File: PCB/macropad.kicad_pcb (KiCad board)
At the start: 2 copper layers, 80.5 x 95.5 mm, 38 parts, among them SW1 Kailh Choc V2, SW10 Kailh Choc V2, SW11 Kailh Choc V2, SW12 Kailh Choc V2, SW13 Kailh Choc V2, SW14 Kailh Choc V2, SW15 Kailh Choc V2, SW16 Kailh Choc V2, SW2 Kailh Choc V2, SW3 Kailh Choc V2, SW4 Kailh Choc V2, SW5 Kailh Choc V2, SW6 Kailh Choc V2, SW7 Kailh Choc V2, SW8 Kailh Choc V2, SW9 Kailh Choc V2, U2 SEEEDUINO XIAO RP2040

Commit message: Finish firmware + misc updates
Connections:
- Brd1 pad 2: +3.3V -> +5V
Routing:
- net +3.3V: track 28.4 -> 16.6 mm
- net +5V: track 76.7 -> 77.7 mm, vias 3 -> 2
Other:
- board text added: "Rev 5.2"
- board text removed: "Rev 5.1"
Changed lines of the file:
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@@
     (title "Cyao macropad")
     (date "2024-09-23")
-    (rev "v5.1")
+    (rev "v5.2")
     (company "Cheyao")
     (comment 1 "https://github.com/cheyao/macropad")
@@
       (net 26 "GND") (pinfunction "GND") (pintype "input"))
     (pad "2" thru_hole oval (at -1.08 -10.6 90) (size 2 1.6) (drill 1) (layers "*.Cu" "*.Mask")
-      (net 25 "+3.3V") (pinfunction "VCC") (pintype "input"))
+      (net 27 "+5V") (pinfunction "VCC") (pintype "input"))
     (pad "3" thru_hole oval (at 1.46 -10.6 90) (size 2 1.6) (drill 1) (layers "*.Cu" "*.Mask")
       (net 29 "Net-(Brd1-SCL)") (pinfunction "SCL") (pintype "input"))
@@
   (gr_line (start 185 145.5) (end 185 50)
     (stroke (width 0.05) (type default)) (layer "Edge.Cuts"))
-  (gr_text "Rev 5.1\n" (at 109.5 64.5) (layer "Eco2.User")
+  (gr_text "Rev 5.2\n\n" (at 109.5 69.25) (layer "Eco2.User")
     (effects (font (size 3 3) (thickness 0.3)) (justify left bottom))
   )
@@
   (segment (start 154 92.75) (end 152 92.75) (width 0.45) (layer "F.Cu") (net 5))
   (segment (start 179.46 60.46) (end 175.75 60.46) (width 0.45) (layer "F.Cu") (net 5))
-  (segment (start 177.12 95) (end 177.5 95) (width 0.45) (layer "F.Cu") (net 5))
   (segment (start 170.5 92.75) (end 168.5 92.75) (width 0.45) (layer "F.Cu") (net 5))
   (segment (start 152 92.75) (end 149.75 95) (width 0.45) (layer "F.Cu") (net 5))
@@
   (segment (start 174.16 52.84) (end 175.75 52.84) (width 0.45) (layer "B.Cu") (net 24))
   (segment (start 173.25 69.25) (end 173.25 53.75) (width 0.45) (layer "B.Cu") (net 24))
-  (segment (start 143.46 60.21) (end 146 62.75) (width 0.6) (layer "F.Cu") (net 25))
   (segment (start 146 62.75) (end 148.69 62.75) (width 0.6) (layer "F.Cu") (net 25))
   (segment (start 148.69 62.75) (end 148.75 62.81) (width 0.6) (layer "F.Cu") (net 25))
-  (segment (start 143.46 52) (end 143.46 60.21) (width 0.6) (layer "F.Cu") (net 25))
-  (segment (start 154.83 57.92) (end 160.5 57.92) (width 0.6) (layer "B.Cu") (net 25))
-  (segment (start 149.94 62.81) (end 154.83 57.92) (width 0.6) (layer "B.Cu") (net 25))
-  (segment (start 148.75 62.81) (end 149.94 62.81) (width 0.6) (layer "B.Cu") (net 25))
-  (segment (start 172.1 74.25) (end 172.2 74.15) (width 0.6) (layer "F.Cu") (net 26))
+  (segment (start 148.75 62.81) (end 150.94 62.81) (width 0.6) (layer "B.Cu") (net 25))
+  (segment (start 155.83 57.92) (end 160.5 57.92) (width 0.6) (layer "B.Cu") (net 25))
+  (segment (start 150.94 62.81) (end 155.83 57.92) (width 0.6) (layer "B.Cu") (net 25))
   (segment (start 126.45 73.8) (end 128 72.25) (width 0.6) (layer "F.Cu") (net 26))
   (segment (start 125.5 73.8) (end 126.45 73.8) (width 0.6) (layer "F.Cu") (net 26))
@@
   (via (at 171.5 60.5) (size 1) (drill 0.5) (layers "F.Cu" "B.Cu") (net 26))
   (via (at 172.25 72.75) (size 1) (drill 0.5) (layers "F.Cu" "B.Cu") (net 26))
+  (segment (start 140.92 56.42) (end 143.75 59.25) (width 0.6) (layer "B.Cu") (net 26))
   (segment (start 128 69.34) (end 140.92 56.42) (width 0.6) (layer "B.Cu") (net 26))
   (segment (start 128 72.25) (end 128 69.34) (width 0.6) (layer "B.Cu") (net 26))
-  (segment (start 154.12 55.38) (end 150.25 59.25) (width 0.6) (layer "B.Cu") (net 26))
-  (segment (start 143.75 59.25) (end 140.92 56.42) (width 0.6) (layer "B.Cu") (net 26))
+  (segment (start 143.75 59.25) (end 151 59.25) (width 0.6) (layer "B.Cu") (net 26))
   (segment (start 171.5 71.900002) (end 171.5 72) (width 0.6) (layer "B.Cu") (net 26))
+  (segment (start 154.87 55.38) (end 160.5 55.38) (width 0.6) (layer "B.Cu") (net 26))
   (segment (start 171.5 72) (end 172.25 72.75) (width 0.6) (layer "B.Cu") (net 26))
   (segment (start 140.92 56.42) (end 140.92 52) (width 0.6) (layer "B.Cu") (net 26))
-  (segment (start 150.25 59.25) (end 143.75 59.25) (width 0.6) (layer "B.Cu") (net 26))
-  (segment (start 160.5 55.38) (end 154.12 55.38) (width 0.6) (layer "B.Cu") (net 26))
+  (segment (start 151 59.25) (end 154.87 55.38) (width 0.6) (layer "B.Cu") (net 26))
   (segment (start 171.5 60.5) (end 171.5 71.900002) (width 0.6) (layer "B.Cu") (net 26))
-  (segment (start 156.66 52.84) (end 160.5 52.84) (width 0.6) (layer "F.Cu") (net 27))
   (segment (start 120.6 70.5) (end 120.6 69.9) (width 0.6) (layer "F.Cu") (net 27))
+  (segment (start 120.6 69.9) (end 134.29 56.21) (width 0.6) (layer "F.Cu") (net 27))
   (segment (start 169.25 68.75) (end 169.25 68.9) (width 0.6) (layer "F.Cu") (net 27))
   (segment (start 169.25 68.9) (end 167.3 70.85) (width 0.6) (layer "F.Cu") (net 27))
-  (segment (start 120.6 69.9) (end 122 68.5) (width 0.6) (layer "F.Cu") (net 27))
-  (segment (start 155.5 54) (end 156.66 52.84) (width 0.6) (layer "F.Cu") (net 27))
-  (segment (start 124.5 66) (end 149.75 66) (width 0.6) (layer "F.Cu") (net 27))
-  (segment (start 155.5 61.25) (end 155.5 54) (width 0.6) (layer "F.Cu") (net 27))
-  (segment (start 122 68.5) (end 124.5 66) (width 0.6) (layer "F.Cu") (net 27))
-  (via (at 149.75 66) (size 1) (drill 0.5) (layers "F.Cu" "B.Cu") (net 27))
-  (via (at 155.5 61.25) (size 1) (drill 0.5) (layers "F.Cu" "B.Cu") (net 27))
+  (segment (start 134.29 56.21) (end 143.46 56.21) (width 0.6) (layer "F.Cu") (net 27))
+  (via (at 143.46 56.21) (size 1) (drill 0.5) (layers "F.Cu" "B.Cu") (net 27))
   (via (at 169.25 68.75) (size 1) (drill 0.5) (layers "F.Cu" "B.Cu") (net 27))
+  (segment (start 155.16 52.84) (end 160.5 52.84) (width 0.6) (layer "B.Cu") (net 27))
   (segment (start 164.59 52.84) (end 160.5 52.84) (width 0.6) (layer "B.Cu") (net 27))
-  (segment (start 150.75 66) (end 155.5 61.25) (width 0.6) (layer "B.Cu") (net 27))
   (segment (start 169.25 57.5) (end 164.59 52.84) (width 0.6) (layer "B.Cu") (net 27))
-  (segment (start 149.75 66) (end 150.75 66) (width 0.6) (layer "B.Cu") (net 27))
+  (segment (start 143.46 56.21) (end 144.75 57.5) (width 0.6) (layer "B.Cu") (net 27))
+  (segment (start 144.75 57.5) (end 150.5 57.5) (width 0.6) (layer "B.Cu") (net 27))
+  (segment (start 143.46 52) (end 143.46 56.21) (width 0.6) (layer "B.Cu") (net 27))
+  (segment (start 150.5 57.5) (end 155.16 52.84) (width 0.6) (layer "B.Cu") (net 27))
   (segment (start 169.25 68.75) (end 169.25 57.5) (width 0.6) (layer "B.Cu") (net 27))
   (segment (start 151.25 56.25) (end 153.75 58.75) (width 0.45) (layer "F.Cu") (net 28))

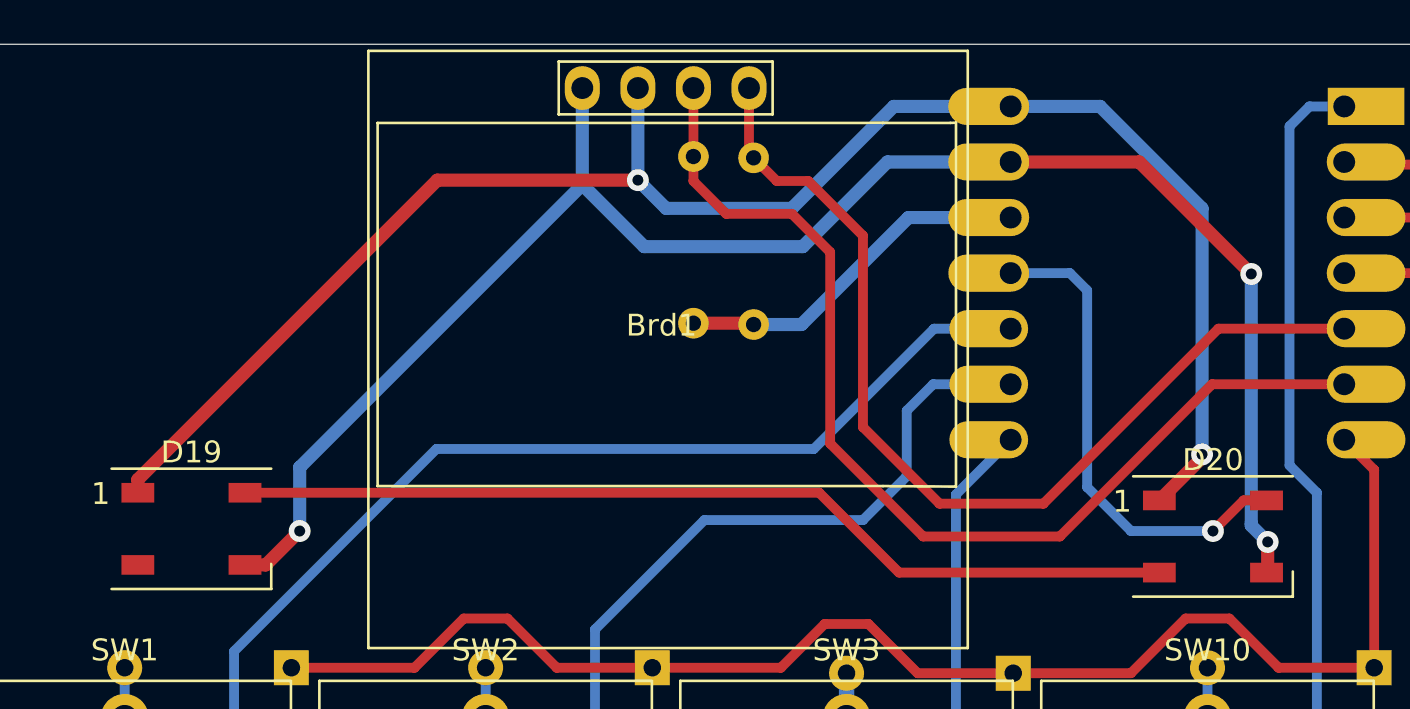
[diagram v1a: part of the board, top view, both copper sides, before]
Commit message: Add decoupling capacitors & verified footprints
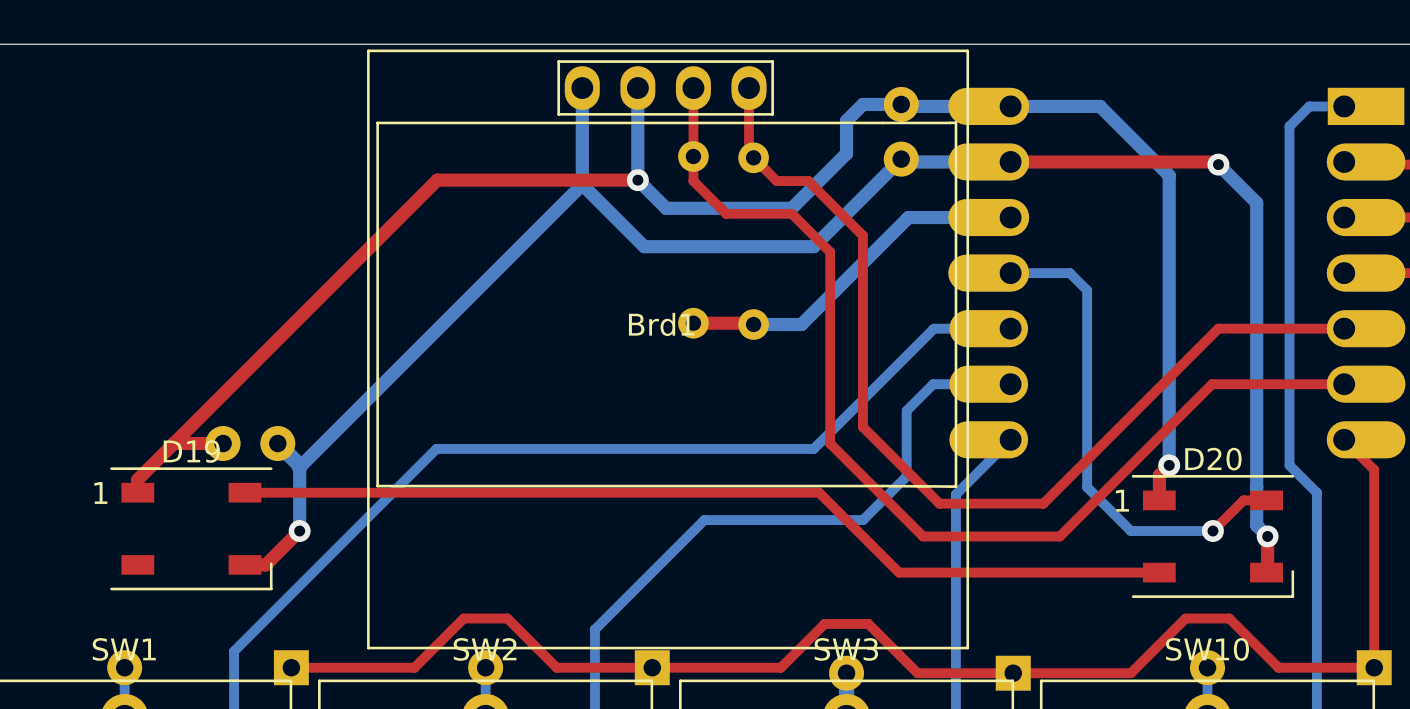
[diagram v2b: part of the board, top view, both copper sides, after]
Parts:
- added C1: 10pF, Capacitor_THT:C_Disc_D3.0mm_W1.6mm_P2.50mm, B.Cu at (124.5, 68.2)
- added C2: 1uF, Capacitor_THT:C_Disc_D3.0mm_W1.6mm_P2.50mm, B.Cu at (155.5, 52.8)
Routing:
- net GND: track 78.2 -> 81.9 mm
- net +5V: track 77.7 -> 79.6 mm
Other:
- board text added: "Rev 5.3"
- board text removed: "Rev 5.2"

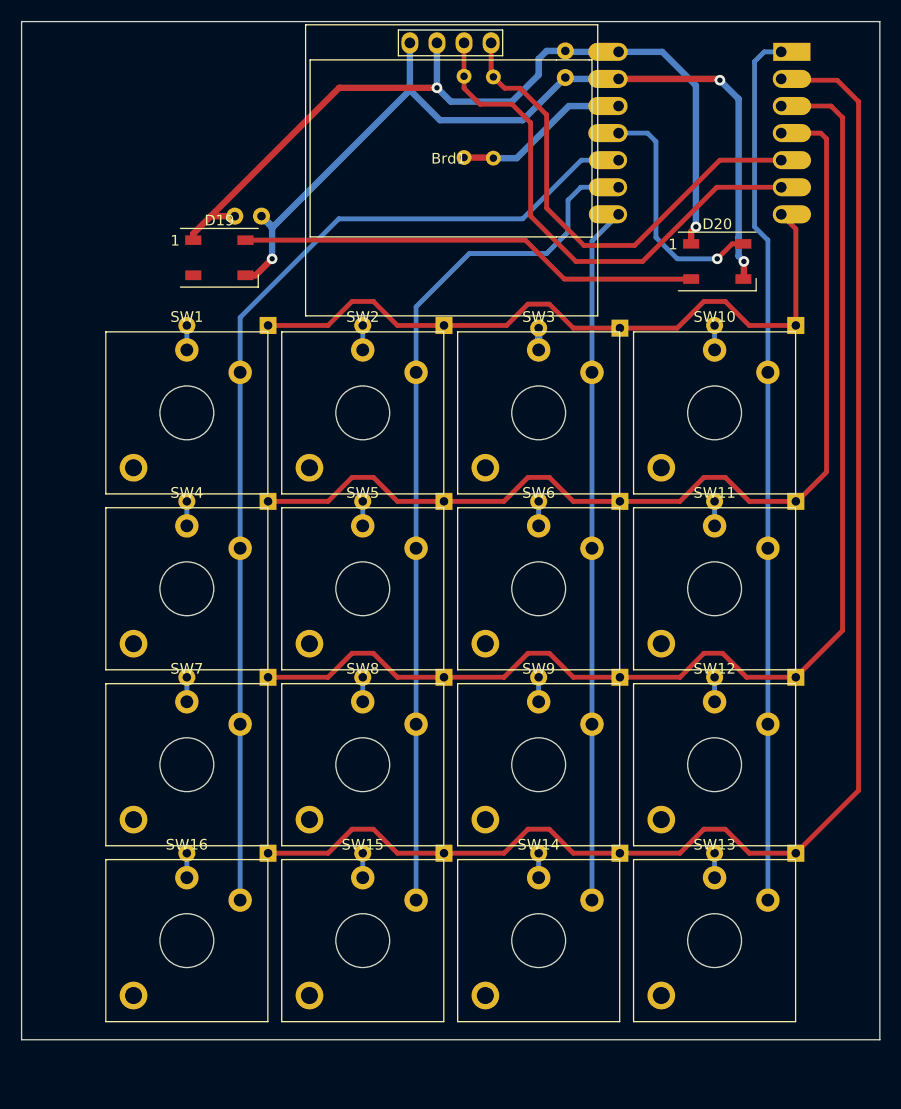
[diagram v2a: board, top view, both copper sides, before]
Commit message: Revamp switch margins
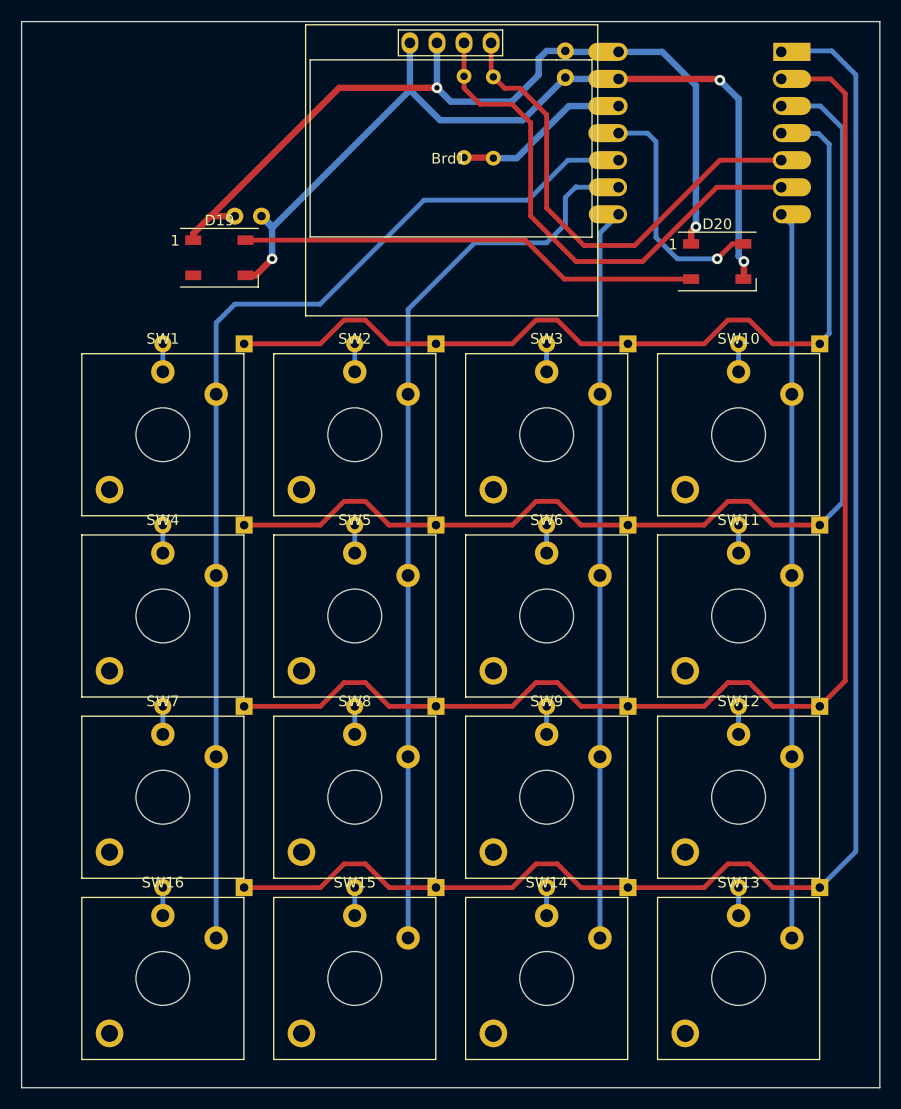
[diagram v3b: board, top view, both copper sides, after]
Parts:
- SW1, SW10, SW11, SW12, SW13, SW14, SW15, SW16, SW2, SW3, SW4, SW5, SW6, SW7, SW8, SW9: footprint key:SW_Kailh_Choc_V2 -> key:SW_Kailh_Choc_V2_1.00u
- moved SW13 4.20 mm to (171.8, 139.8)
- moved SW16 4.20 mm to (117.8, 139.8)
- moved D13 3.93 mm to (179.4, 131.2)
- moved D16 3.93 mm to (125.4, 131.2)
- moved SW12 3.79 mm to (171.8, 122.8)
- moved SW7 3.79 mm to (117.8, 122.8)
- moved SW14 3.63 mm to (153.8, 139.8)
- moved SW15 3.63 mm to (135.8, 139.8)
- moved D12 3.53 mm to (179.4, 114.2)
- moved D7 3.53 mm to (125.4, 114.2)
- moved SW11 3.40 mm to (171.8, 105.8)
- moved SW4 3.40 mm to (117.8, 105.8)
- moved D14 3.31 mm to (161.4, 131.2)
- moved D15 3.31 mm to (143.4, 131.2)
- moved D11 3.16 mm to (179.4, 97.2)
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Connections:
- U2 pad 1: COL3 -> ROW3
- U2 pad 2: ROW3 -> ROW2
- U2 pad 3: ROW2 -> ROW1
- U2 pad 4: ROW1 -> ROW0
- U2 pad 7: ROW0 -> COL3
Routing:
- net ROW0: track 66.1 -> 83.6 mm
- net COL3: track 82.0 -> 68.3 mm
- net ROW1: track 94.8 -> 104.2 mm
- net ROW3: track 136.2 -> 145.1 mm
- net ROW2: track 115.6 -> 124.6 mm
- net COL0: track 96.3 -> 101.8 mm
- net COL1: track 81.1 -> 84.9 mm
- net COL2: track 65.4 -> 68.6 mm
- net Net-(D3-A): track 2.05 -> 2.62 mm
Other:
- board size 80.5 x 95.5 mm -> 80.5 x 100 mm
- board text added: "Rev 6.0"
- board text removed: "Rev 5.3"

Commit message: Added backlights
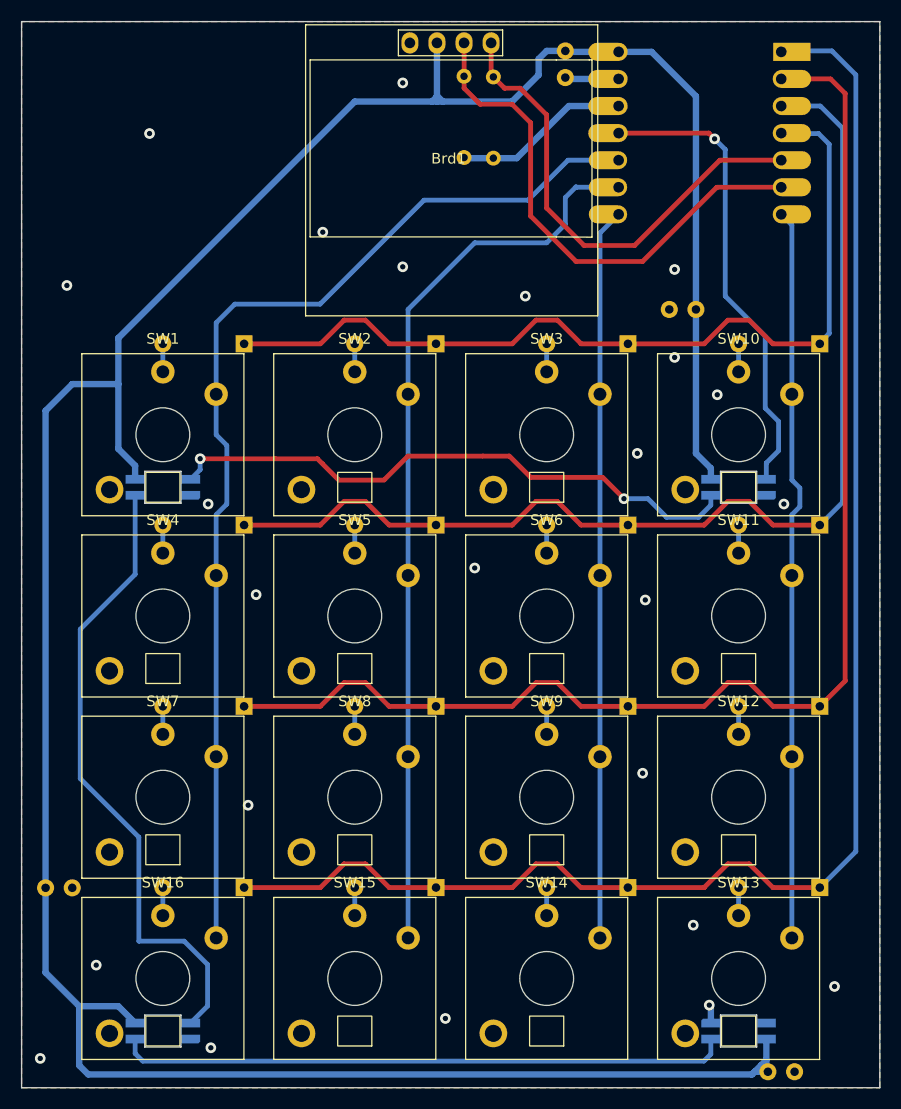
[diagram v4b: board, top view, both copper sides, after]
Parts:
- removed D19, D20: WS2812B, LED_SMD:LED_WS2812B_PLCC4_5.0x5.0mm_P3.2mm
- added C3: 10pF, Capacitor_THT:C_Disc_D3.0mm_W1.6mm_P2.50mm, B.Cu at (106.8, 131.2)
- added C4: 10pF, Capacitor_THT:C_Disc_D3.0mm_W1.6mm_P2.50mm, B.Cu at (167.8, 77.0)
- added D17: SK6812MINI, LED:SK6812MINI-E, B.Cu at (171.8, 93.7)
- added D18: SK6812MINI, LED:SK6812MINI-E, B.Cu at (117.8, 93.7)
- added D21: SK6812MINI, LED:SK6812MINI-E, B.Cu at (117.8, 144.7)
- added D22: SK6812MINI, LED:SK6812MINI-E, B.Cu at (171.8, 144.7)
- moved C1 94.6 mm to (174.5, 148.5)
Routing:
- net +5V: track 79.6 -> 272.8 mm, vias 2 -> 0
- net GND: track 81.9 -> 6.80 mm, vias 3 -> 24
- net Net-(D18-DOUT): track 0.00 -> 59.7 mm
- net Net-(D21-DOUT): track 0.00 -> 57.3 mm
- net Net-(D17-DOUT): track 0.00 -> 55.7 mm, vias 0 -> 2
- net Net-(D19-DIN): track 43.3 -> 0.00 mm
- net LED: track 22.4 -> 44.1 mm
- net COL0: track 101.8 -> 102.6 mm
- net COL3: track 68.3 -> 68.9 mm
- added copper zone on B.Cu, net GND
- added copper zone on F.Cu, net GND
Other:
- board text added: "Rev 7.1"
- board text removed: "Rev 6.0"

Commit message: Add silkscreens and misc improvements
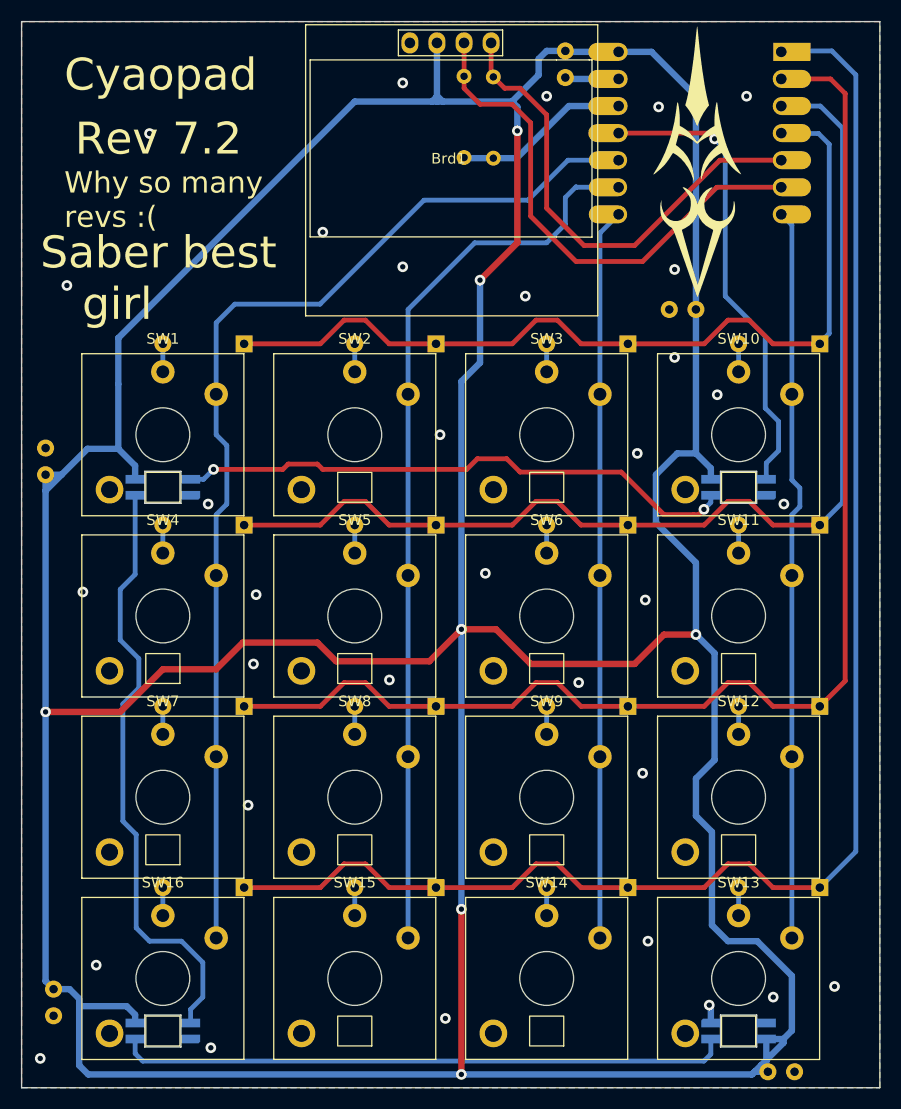
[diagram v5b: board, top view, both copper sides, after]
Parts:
- added C5: 10pF, Capacitor_THT:C_Disc_D3.0mm_W1.6mm_P2.50mm, B.Cu at (106.8, 92.5)
- added G***: LOGO, LOGO, F.Cu at (167.8, 63.0)
- moved C3 9.53 mm to (107.5, 140.8), turned to -90 degrees
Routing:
- net +5V: track 272.8 -> 502.4 mm, vias 0 -> 7
- net Net-(D18-DOUT): track 59.7 -> 56.8 mm
- net Net-(D17-DOUT): track 55.7 -> 53.3 mm
- net GND: vias 24 -> 33
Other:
- board text added: "Rev 7.2"
- board text added: "Saber best girl"
- board text removed: "Rev 7.1"
